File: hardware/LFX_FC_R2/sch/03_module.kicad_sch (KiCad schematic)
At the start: 9 parts, among them J4 SM04B-SRSS-TB, U7 TPD4E05U06DQA

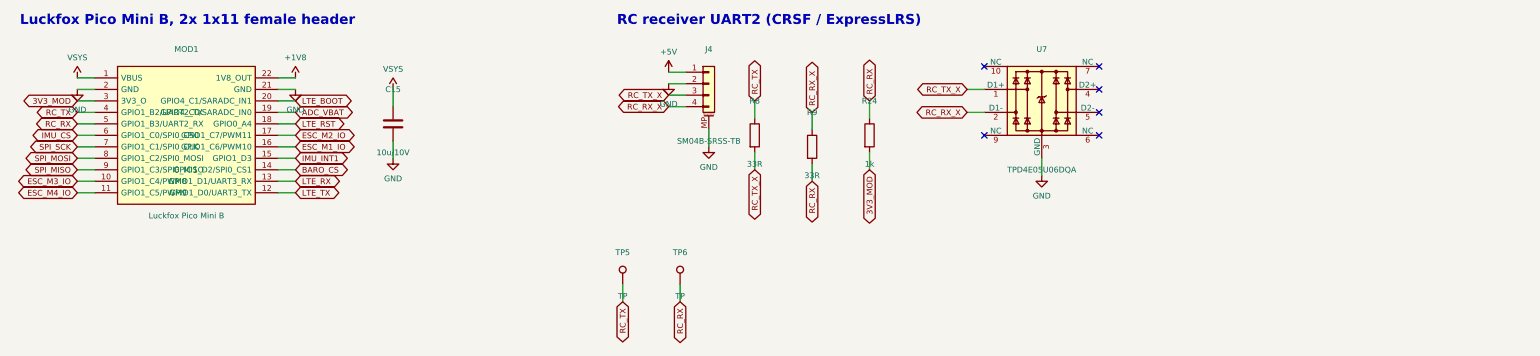
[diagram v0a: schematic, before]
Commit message: hardware: LFX_FC_R2 GPS port J18 (ATGM336H / NEO-M8N class) on UART5
- J18: JST-SH 4-pin at the left edge, 1 +5V, 2 GND, 3 NC, 4 module TXD ->
  board RX.  MOD1 pin 14 (GPIO1_D2) becomes UART5_RX_M1, 33R + TPD1E05U06 ESD.
- Baro chip select moves to pin 15 (GPIO1_D3, MCU GPIO); IMU INT1 dropped
  (polled).
- +5V to J18 hand-routed from J4 on B.Cu along the board edge (x 0.75), so it
  walls nothing in.
- Hand routes for the connections the router kept leaving open: SIM RST/CLK
  (U12 channels swapped so they no longer cross), BUZ_CTRL, the U2 +5V
  escape, LTE_1V8 between U9/U10 (paths taken from dc53508).
- gen_sch keeps the board rules in kicad_pro; clean_stubs removes dangling
  vias; Freerouting runs as a background UI element on macOS.
- DRC: 0 violations, 0 unconnected, schematic parity clean; ERC 0.

Co-Authored-By: Claude Opus 5.5 <noreply@anthropic.com>
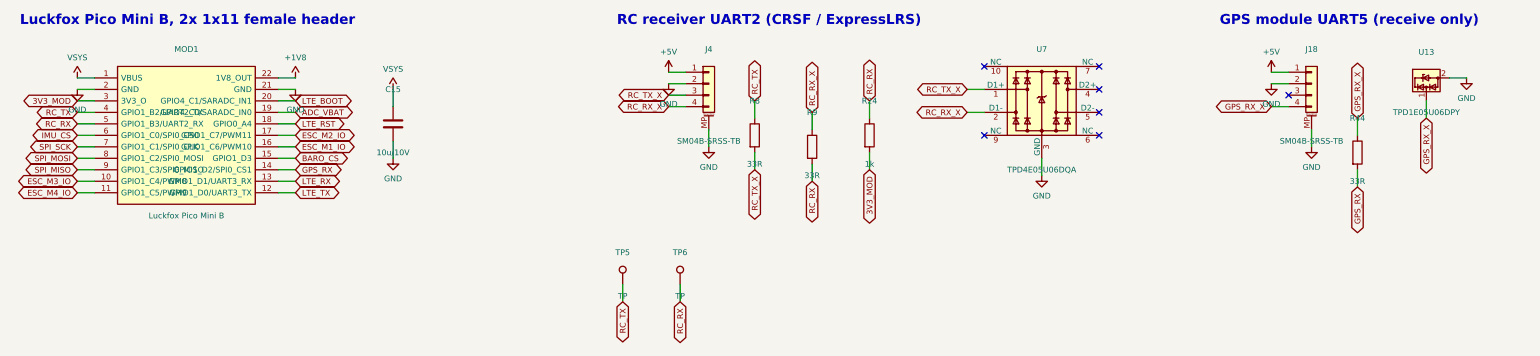
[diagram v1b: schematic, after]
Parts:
- added J18: SM04B-SRSS-TB, Connector_JST:JST_SH_SM04B-SRSS-TB_1x04-1MP_P1.00mm_Horizontal, symbol Connector_Generic_MountingPin:Conn_01x04_MountingPin
- added R44: 33R, Resistor_SMD:R_0402_1005Metric, symbol Device:R
- added U13: TPD1E05U06DPY, Package_SON:Texas_DPY0002A_0.6x1mm_P0.65mm, symbol Power_Protection:TPD1E05U06DPY
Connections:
- net IMU_INT1 is gone; now on net BARO_CS: MOD1.15 (GPIO1_D3)
- net +5V: now also J18.1 (Pin_1)
- net BARO_CS: no longer MOD1.14 (GPIO1_D2/SPI0_CS1)
- net GND: now also J18.2 (Pin_2), J18.MP (MountPin), U13.2 (GND)
- new net GPS_RX: MOD1.14 (GPIO1_D2/SPI0_CS1), R44.2
- new net GPS_RX_X: J18.4 (Pin_4), R44.1, U13.1 (I/O)
- no-connect marks 6 -> 7
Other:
- note added: "GPS module UART5 (receive only)"

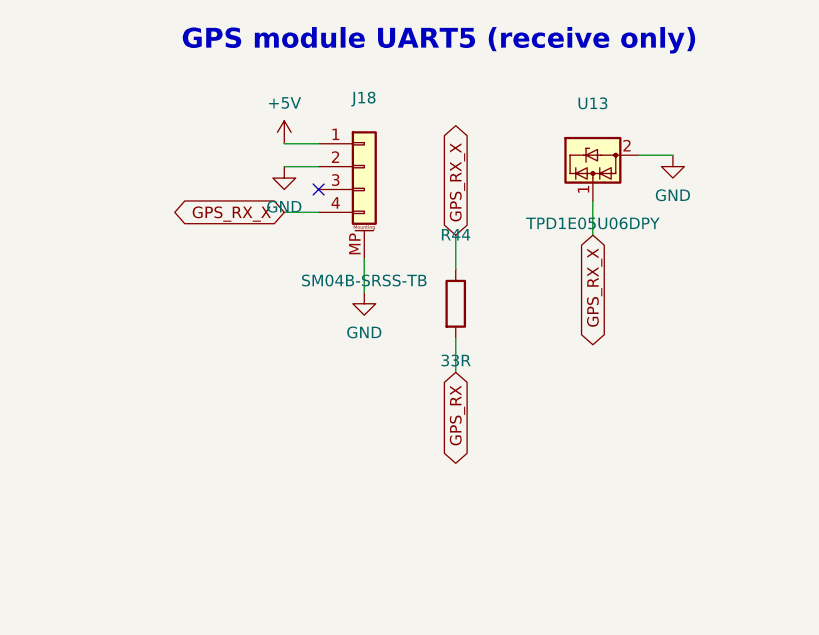
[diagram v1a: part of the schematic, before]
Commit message: hardware: LFX_FC_R2 J18 as a 5-pin 2.54 mm header for the ATGM336H module
The JST-SH 4 GPS port becomes a right-angle 1x05 header at the left edge,
pin for pin with the 5-pin ATGM336H module (VCC GND TXD RXD PPS), so a
straight Dupont lead plugs in. Module TXD goes to UART5_RX as before;
RXD and PPS stay open (no Luckfox pins left).

New LFX footprint PinHeader_1x05_P2.54mm_EdgeHorizontal (stock 3D model
turned 180 degrees). Probe pads TP8/TP9 move to the bottom beside it.
Board edited in place from the routed R2: DRC 0 / unconnected 0 /
parity 0, ERC 0. 3D renders refreshed.

Co-Authored-By: Claude Opus 5.5 <noreply@anthropic.com>
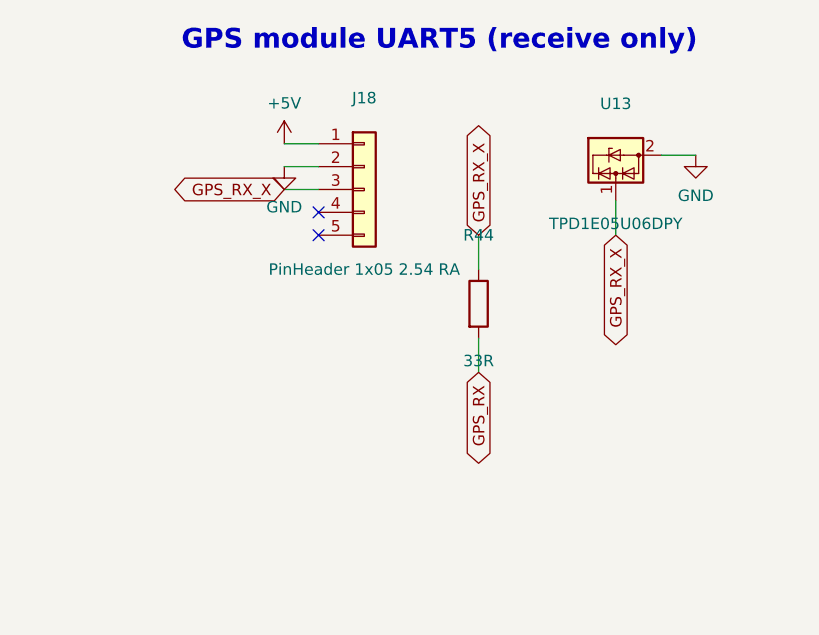
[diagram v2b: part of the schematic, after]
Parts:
- J18: value SM04B-SRSS-TB -> PinHeader 1x05 2.54 RA; footprint Connector_JST:JST_SH_SM04B-SRSS-TB_1x04-1MP_P1.00mm_Horizontal -> LFX:PinHeader_1x05_P2.54mm_EdgeHorizontal; symbol Connector_Generic_MountingPin:Conn_01x04_MountingPin -> Connector_Generic:Conn_01x05
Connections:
- net GND: no longer J18.MP (MountPin)
- net GPS_RX_X: now also J18.3 (Pin_3); no longer J18.4 (Pin_4)
- no-connect marks 7 -> 8
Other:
- moved on the sheet: R44, U13
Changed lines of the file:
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@@
 	)
 	(symbol
-		(lib_id "Connector_Generic_MountingPin:Conn_01x04_MountingPin")
-		(at 302.26 39.37 0)
+		(lib_id "Connector_Generic:Conn_01x05")
+		(at 302.26 41.91 0)
 		(unit 1)
 		(exclude_from_sim no) (in_bom yes) (on_board yes)
@@
 			(effects (font (size 1.27 1.27)))
 		)
-		(property "Value" "SM04B-SRSS-TB"
-			(at 302.26 52.07 0)
-			(effects (font (size 1.27 1.27)))
-		)
-		(property "Footprint" "Connector_JST:JST_SH_SM04B-SRSS-TB_1x04-1MP_P1.00mm_Horizontal"
-			(at 302.26 39.37 0)
+		(property "Value" "PinHeader 1x05 2.54 RA"
+			(at 302.26 50.8 0)
+			(effects (font (size 1.27 1.27)))
+		)
+		(property "Footprint" "LFX:PinHeader_1x05_P2.54mm_EdgeHorizontal"
+			(at 302.26 41.91 0)
 			(effects (font (size 1.27 1.27)) (hide yes))
 		)
 		(property "Datasheet" ""
-			(at 302.26 39.37 0)
-			(effects (font (size 1.27 1.27)) (hide yes))
-		)
-		(property "Description" "GPS module (ATGM336H / NEO-M8N class). 1:5V 2:GND 3:NC (module RXD - no board TX) 4:module TXD -> board RX (UART5)"
-			(at 302.26 39.37 0)
+			(at 302.26 41.91 0)
+			(effects (font (size 1.27 1.27)) (hide yes))
+		)
+		(property "Description" "ATGM336H GPS module, pin for pin: 1:VCC 5V 2:GND 3:module TXD -> board RX (UART5) 4:module RXD (open) 5:PPS (open)"
+			(at 302.26 41.91 0)
 			(effects (font (size 1.27 1.27)) (hide yes))
 		)
@@
 		(pin "3")
 		(pin "4")
-		(pin "MP")
+		(pin "5")
 		(instances
 			(project "LFX_FC_R2"
@@
 		)
 	)
+	(wire
+		(pts (xy 297.18 41.91) (xy 293.37 41.91))
+		(stroke (width 0) (type default))
+	)
+	(global_label "GPS_RX_X"
+		(shape bidirectional)
+		(at 293.37 41.91 180)
+		(effects (font (size 1.27 1.27)) (justify right))
+		(property "Intersheetrefs" "${INTERSHEET_REFS}"
+			(at 293.37 41.91 0)
+			(effects (font (size 1.27 1.27)) (hide yes))
+		)
+	)
 	(no_connect
-		(at 297.18 41.91)
-	)
-	(wire
-		(pts (xy 297.18 44.45) (xy 293.37 44.45))
-		(stroke (width 0) (type default))
-	)
-	(global_label "GPS_RX_X"
-		(shape bidirectional)
-		(at 293.37 44.45 180)
-		(effects (font (size 1.27 1.27)) (justify right))
-		(property "Intersheetrefs" "${INTERSHEET_REFS}"
-			(at 293.37 44.45 0)
-			(effects (font (size 1.27 1.27)) (hide yes))
-		)
-	)
-	(wire
-		(pts (xy 302.26 49.53) (xy 302.26 53.34))
-		(stroke (width 0) (type default))
-	)
-	(symbol
-		(lib_id "power:GND")
-		(at 302.26 53.34 0)
-		(unit 1)
-		(exclude_from_sim no) (in_bom no) (on_board yes) (dnp no)
-		(property "Reference" "#PWR0063"
-			(at 302.26 49.53 0)
-			(effects (font (size 1.27 1.27)) (hide yes))
-		)
-		(property "Value" "GND"
-			(at 302.26 57.84 0)
-			(effects (font (size 1.27 1.27)))
-		)
-		(property "Footprint" "" (at 0 0 0) (effects (font (size 1.27 1.27)) (hide yes)))
-		(property "Datasheet" "" (at 0 0 0) (effects (font (size 1.27 1.27)) (hide yes)))
-		(instances
-			(project "LFX_FC_R2"
-				(path "/9564b83f-500d-c692-1cc5-81840b134811/ff557765-04f8-5d0c-aacb-cf31df93a6f3"
-					(reference "#PWR0063") (unit 1)
-				)
-			)
-		)
+		(at 297.18 44.45)
+	)
+	(no_connect
+		(at 297.18 46.99)
 	)
 	(symbol
 		(lib_id "Device:R")
-		(at 312.42 54.61 0)
+		(at 314.96 54.61 0)
 		(unit 1)
 		(exclude_from_sim no) (in_bom yes) (on_board yes)
 		(dnp no)
 		(property "Reference" "R44"
-			(at 312.42 46.99 0)
+			(at 314.96 46.99 0)
 			(effects (font (size 1.27 1.27)))
 		)
 		(property "Value" "33R"
-			(at 312.42 60.96 0)
+			(at 314.96 60.96 0)
 			(effects (font (size 1.27 1.27)))
 		)
 		(property "Footprint" "Resistor_SMD:R_0402_1005Metric"
-			(at 312.42 54.61 0)
+			(at 314.96 54.61 0)
 			(effects (font (size 1.27 1.27)) (hide yes))
 		)
 		(property "Datasheet" ""
-			(at 312.42 54.61 0)
+			(at 314.96 54.61 0)
 			(effects (font (size 1.27 1.27)) (hide yes))
 		)
@@
 	)
 	(wire
-		(pts (xy 312.42 50.8) (xy 312.42 46.99))
+		(pts (xy 314.96 50.8) (xy 314.96 46.99))
 		(stroke (width 0) (type default))
 	)
 	(global_label "GPS_RX_X"
 		(shape bidirectional)
-		(at 312.42 46.99 90)
+		(at 314.96 46.99 90)
 		(effects (font (size 1.27 1.27)) (justify left))
 		(property "Intersheetrefs" "${INTERSHEET_REFS}"
-			(at 312.42 46.99 0)
-			(effects (font (size 1.27 1.27)) (hide yes))
-		)
-	)
-	(wire
-		(pts (xy 312.42 58.42) (xy 312.42 62.23))
+			(at 314.96 46.99 0)
+			(effects (font (size 1.27 1.27)) (hide yes))
+		)
+	)
+	(wire
+		(pts (xy 314.96 58.42) (xy 314.96 62.23))
 		(stroke (width 0) (type default))
 	)
 	(global_label "GPS_RX"
 		(shape bidirectional)
-		(at 312.42 62.23 270)
+		(at 314.96 62.23 270)
 		(effects (font (size 1.27 1.27)) (justify right))
 		(property "Intersheetrefs" "${INTERSHEET_REFS}"
-			(at 312.42 62.23 0)
+			(at 314.96 62.23 0)
 			(effects (font (size 1.27 1.27)) (hide yes))
 		)
@@
 	(symbol
 		(lib_id "Power_Protection:TPD1E05U06DPY")
-		(at 327.66 38.1 0)
+		(at 330.2 38.1 0)
 		(unit 1)
 		(exclude_from_sim no) (in_bom yes) (on_board yes)
 		(dnp no)
 		(property "Reference" "U13"
-			(at 327.66 32.385 0)
+			(at 330.2 32.385 0)
 			(effects (font (size 1.27 1.27)))
 		)
 		(property "Value" "TPD1E05U06DPY"
-			(at 327.66 45.72 0)
+			(at 330.2 45.72 0)
 			(effects (font (size 1.27 1.27)))
 		)
 		(property "Footprint" "Package_SON:Texas_DPY0002A_0.6x1mm_P0.65mm"
-			(at 327.66 38.1 0)
+			(at 330.2 38.1 0)
 			(effects (font (size 1.27 1.27)) (hide yes))
 		)
 		(property "Datasheet" ""
-			(at 327.66 38.1 0)
+			(at 330.2 38.1 0)
 			(effects (font (size 1.27 1.27)) (hide yes))
 		)
 		(property "Description" "ESD at the GPS connector"
-			(at 327.66 38.1 0)
+			(at 330.2 38.1 0)
 			(effects (font (size 1.27 1.27)) (hide yes))
 		)
@@
 	)
 	(wire
-		(pts (xy 327.66 43.18) (xy 327.66 46.99))
+		(pts (xy 330.2 43.18) (xy 330.2 46.99))
 		(stroke (width 0) (type default))
 	)
 	(global_label "GPS_RX_X"
 		(shape bidirectional)
-		(at 327.66 46.99 270)
+		(at 330.2 46.99 270)
 		(effects (font (size 1.27 1.27)) (justify right))
 		(property "Intersheetrefs" "${INTERSHEET_REFS}"
-			(at 327.66 46.99 0)
-			(effects (font (size 1.27 1.27)) (hide yes))
-		)
-	)
-	(wire
-		(pts (xy 332.74 38.1) (xy 336.55 38.1))
+			(at 330.2 46.99 0)
+			(effects (font (size 1.27 1.27)) (hide yes))
+		)
+	)
+	(wire
+		(pts (xy 335.28 38.1) (xy 339.09 38.1))
 		(stroke (width 0) (type default))
 	)
 	(symbol
 		(lib_id "power:GND")
-		(at 336.55 38.1 0)
+		(at 339.09 38.1 0)
 		(unit 1)
 		(exclude_from_sim no) (in_bom no) (on_board yes) (dnp no)
-		(property "Reference" "#PWR0064"
-			(at 336.55 34.29 0)
+		(property "Reference" "#PWR0063"
+			(at 339.09 34.29 0)
 			(effects (font (size 1.27 1.27)) (hide yes))
 		)
 		(property "Value" "GND"
-			(at 336.55 42.6 0)
+			(at 339.09 42.6 0)
 			(effects (font (size 1.27 1.27)))
 		)
@@
 			(project "LFX_FC_R2"
 				(path "/9564b83f-500d-c692-1cc5-81840b134811/ff557765-04f8-5d0c-aacb-cf31df93a6f3"
-					(reference "#PWR0064") (unit 1)
-				)
-			)
+					(reference "#PWR0063") (unit 1)
+				)
+			)
